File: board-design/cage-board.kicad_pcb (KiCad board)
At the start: 2 copper layers, 160 x 160 mm, 34 parts, among them J1 Jack-DC, J10 73131-0240, J11 73131-0240, J12 73131-0240, J13 Conn_01x02, J14 Conn_01x02, J15 Conn_02x13_test_points, J2 Conn_02x17_Ribbon, J3 TB002-500-03BE, J4 73131-0240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

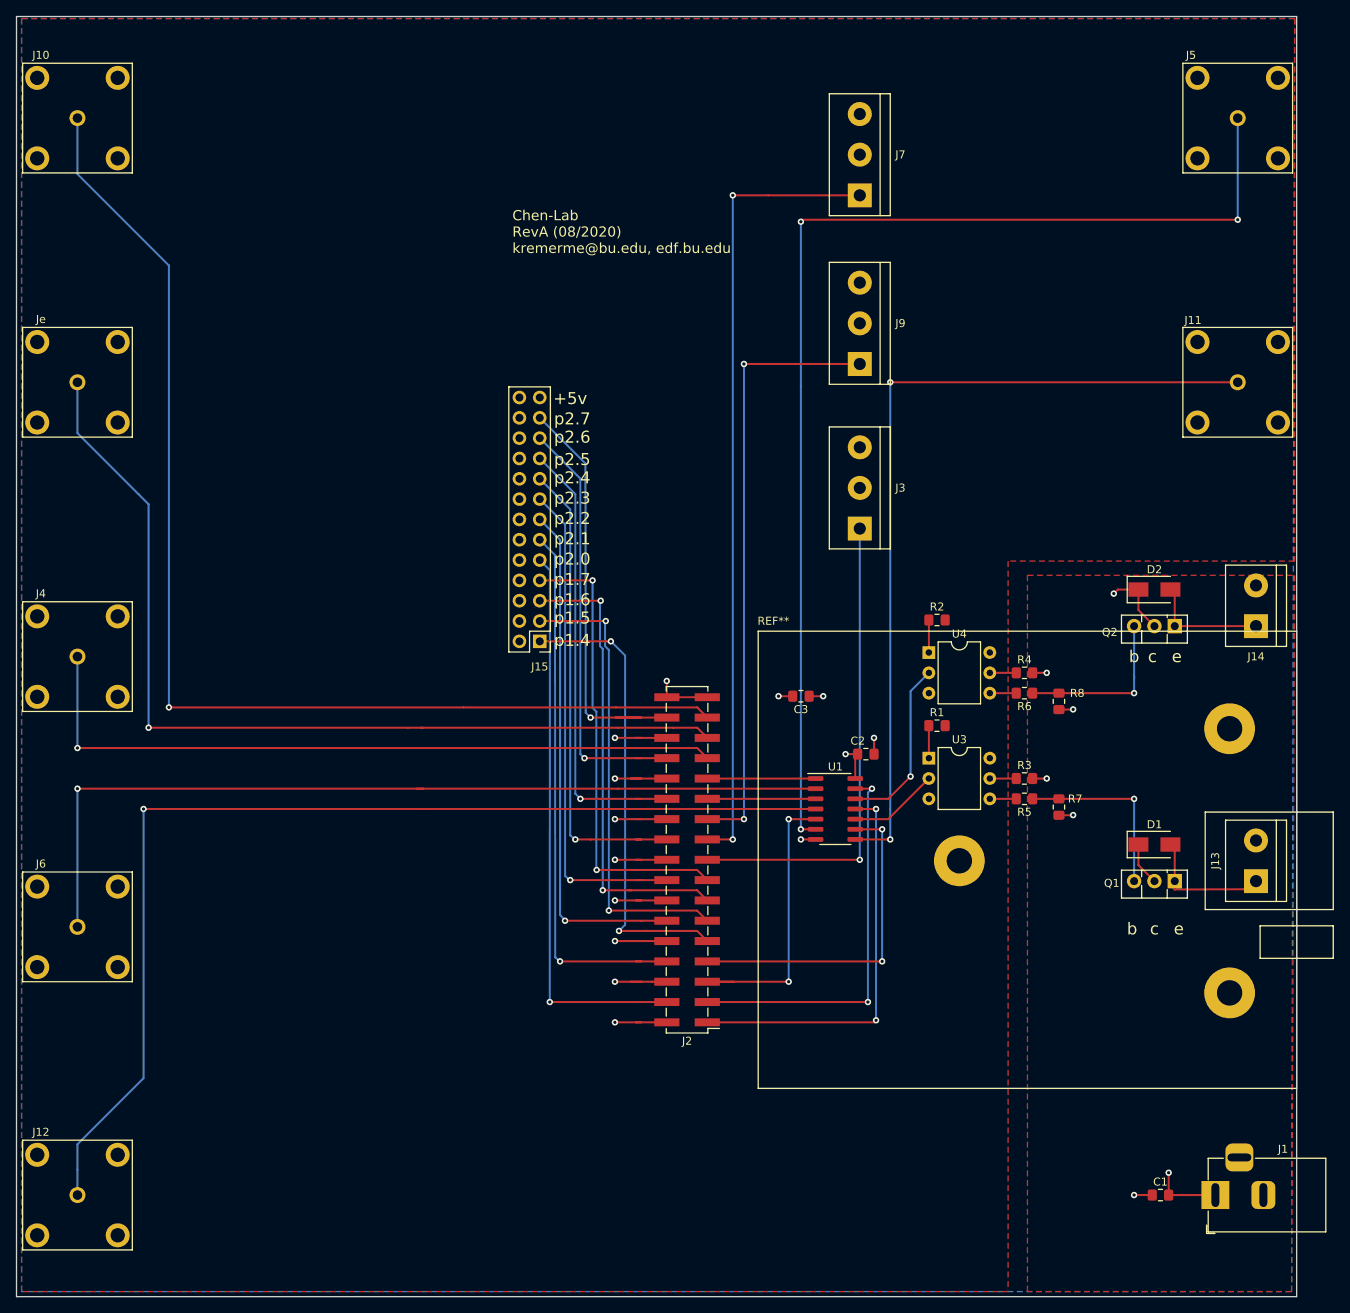
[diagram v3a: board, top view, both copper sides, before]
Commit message: updating schematic, and moving PCB layout forward to RevB
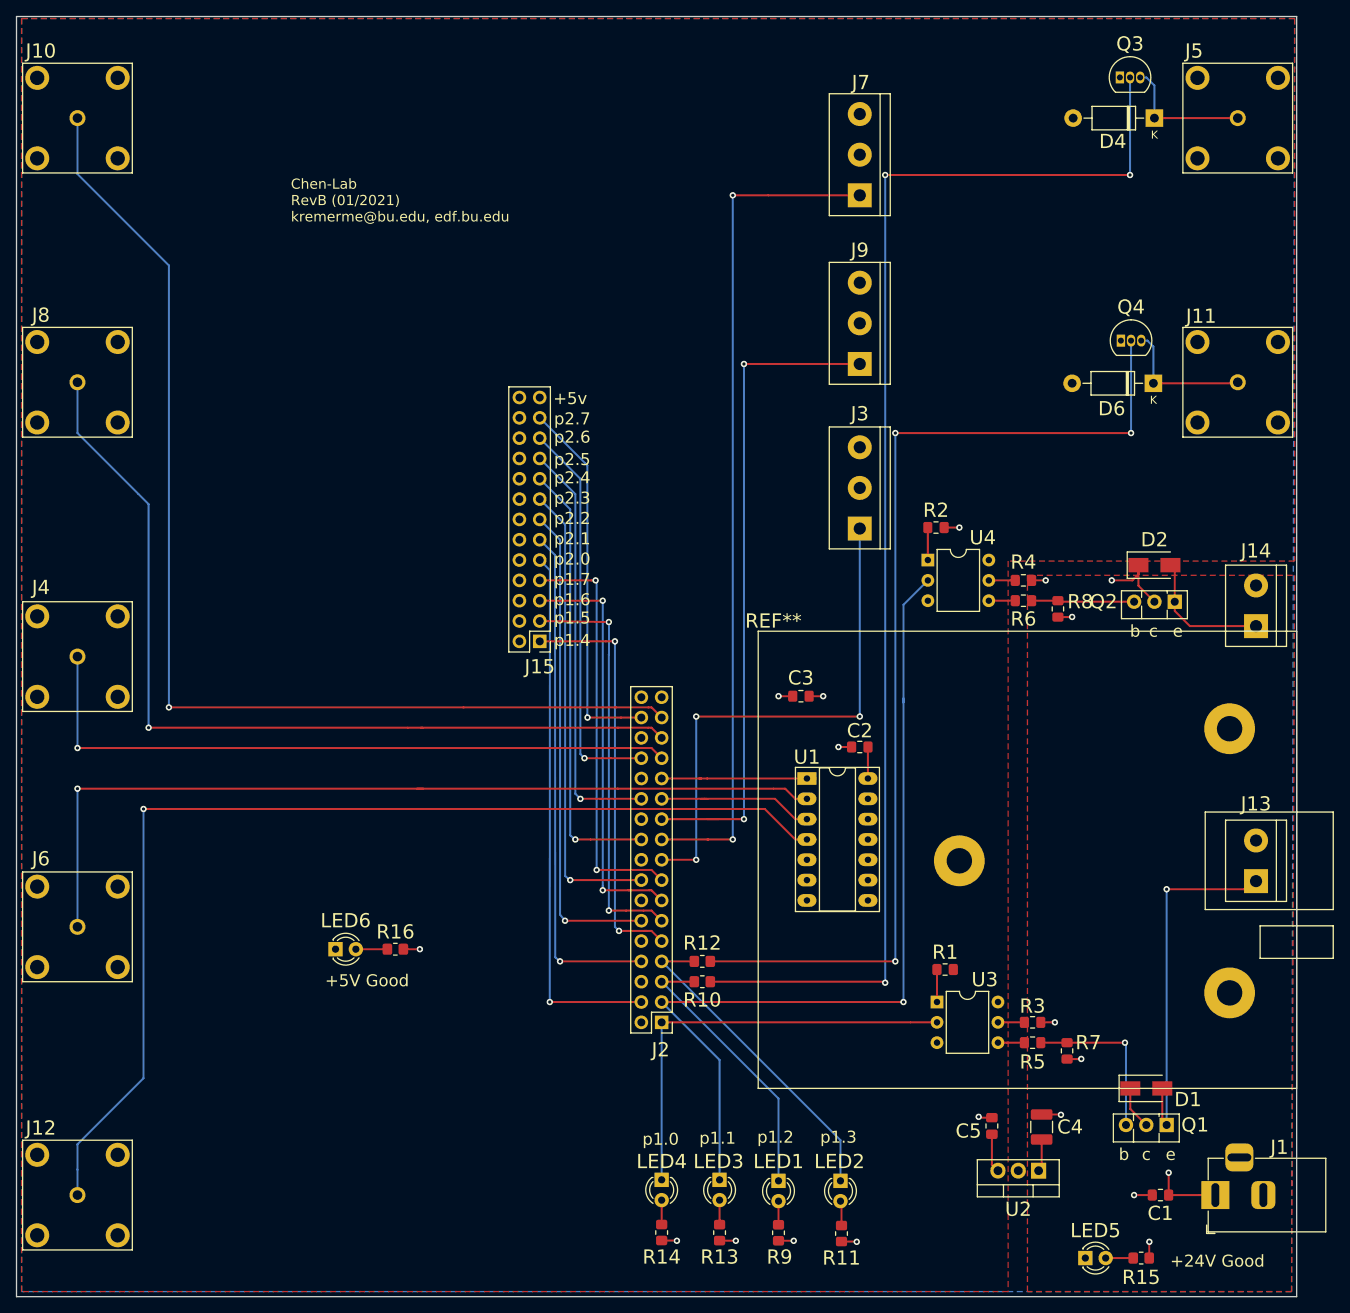
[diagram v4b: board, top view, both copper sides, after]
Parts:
- added C4: 10u 50V, Capacitor_SMD:C_1210_3225Metric_Pad1.33x2.70mm_HandSolder, F.Cu at (171.3, 138.8)
- added C5: 22u 10V, Capacitor_SMD:C_0805_2012Metric_Pad1.18x1.45mm_HandSolder, F.Cu at (165.1, 138.7)
- added D4: 1N4007, Diode_THT:D_DO-41_SOD81_P10.16mm_Horizontal, F.Cu at (185.4, 12.7)
- added D6: 1N4007, Diode_THT:D_DO-41_SOD81_P10.16mm_Horizontal, F.Cu at (185.3, 45.8)
- added LED1: LED, LED_THT:LED_D3.0mm, F.Cu at (138.4, 145.5)
- added LED2: LED, LED_THT:LED_D3.0mm, F.Cu at (146.2, 145.5)
- added LED3: LED, LED_THT:LED_D3.0mm, F.Cu at (131.1, 145.4)
- added LED4: LED, LED_THT:LED_D3.0mm, F.Cu at (123.8, 145.4)
- added LED5: LED, LED_THT:LED_D3.0mm, F.Cu at (176.8, 155.2)
- added LED6: LED, LED_THT:LED_D3.0mm, F.Cu at (83.1, 116.6)
- added Q3: 2N3906, Package_TO_SOT_THT:TO-92_Inline, F.Cu at (181.1, 7.62)
- added Q4: 2N3906, Package_TO_SOT_THT:TO-92_Inline, F.Cu at (181.2, 40.5)
- added R10: R_US, Resistor_SMD:R_0805_2012Metric_Pad1.20x1.40mm_HandSolder, F.Cu at (128.9, 120.7)
- added R11: 200, Resistor_SMD:R_0805_2012Metric_Pad1.20x1.40mm_HandSolder, F.Cu at (146.3, 152.1)
- added R12: R_US, Resistor_SMD:R_0805_2012Metric_Pad1.20x1.40mm_HandSolder, F.Cu at (128.9, 118.1)
- added R13: 200, Resistor_SMD:R_0805_2012Metric_Pad1.20x1.40mm_HandSolder, F.Cu at (131.1, 152.0)
- added R14: 200, Resistor_SMD:R_0805_2012Metric_Pad1.20x1.40mm_HandSolder, F.Cu at (123.8, 152.0)
- added R15: 1k, Resistor_SMD:R_0805_2012Metric_Pad1.20x1.40mm_HandSolder, F.Cu at (183.8, 155.2)
- added R16: 200, Resistor_SMD:R_0805_2012Metric_Pad1.20x1.40mm_HandSolder, F.Cu at (90.5, 116.6)
- added R9: 200, Resistor_SMD:R_0805_2012Metric_Pad1.20x1.40mm_HandSolder, F.Cu at (138.4, 152.0)
- added U2: VX7805-500, Package_TO_SOT_THT:TO-220-3_Vertical, F.Cu at (170.9, 144.3)
- J2: footprint Connector_PinHeader_2.54mm:PinHeader_2x17_P2.54mm_Vertical_SMD -> Connector_PinHeader_2.54mm:PinHeader_2x17_P2.54mm_Vertical
- U1: value 74LS06 -> 74HC04; footprint Package_SO:SOIC-14_3.9x8.7mm_P1.27mm -> Package_DIP:DIP-14_W7.62mm_Socket_LongPads
- U3, U4: value ERJ-UP8F6200V -> 4N25
- moved D1 30.5 mm to (184.4, 134.0)
- moved R1 30.5 mm to (159.3, 119.1)
- moved R3 30.5 mm to (170.2, 125.7)
- moved R5 30.5 mm to (170.2, 128.3)
- moved U3 30.5 mm to (158.2, 123.2)
- moved Q1 30.5 mm to (186.9, 138.6)
- moved R7 30.5 mm to (174.5, 129.3)
- moved J2 20.6 mm to (123.8, 125.7)
- moved R4 11.6 mm to (169.0, 70.5)
- moved R8 11.6 mm to (173.4, 74.0)
- moved U4 11.6 mm to (157.1, 67.9)
- moved R2 11.6 mm to (158.1, 63.9)
- moved R6 11.6 mm to (169.0, 73.0)
- moved U1 5.21 mm to (142.0, 95.2)
- moved D2 3.05 mm to (185.4, 68.6)
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- renumbered Je to J8
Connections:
- J11 pad 1: Net-(J11-Pad1) -> Net-(D6-Pad1)
- J2 pad 33: +5V -> Net-(J2-Pad33)
- J2 pad 34: +5V -> Net-(J2-Pad34)
- J5 pad 1: Net-(J5-Pad1) -> Net-(D4-Pad1)
- U1 pad 11: /P1.0 -> GND
- U1 pad 13: /P1.1 -> GND
- U1 pad 5: /P1.2 -> GND
- U1 pad 6: Net-(J5-Pad1) -> Net-(U1-Pad6)
- U1 pad 8: Net-(J11-Pad1) -> Net-(U1-Pad8)
- U1 pad 9: /P1.3 -> GND
- U3 pad 2: Net-(U1-Pad10) -> /P1.0
- U4 pad 2: Net-(U1-Pad12) -> /P1.1
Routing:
- net Net-(Q3-Pad2): track 0.00 -> 166.3 mm, vias 0 -> 3
- net Net-(J5-Pad1): track 145.2 -> 0.00 mm, vias 3 -> 0
- net Net-(Q4-Pad2): track 0.00 -> 130.8 mm, vias 0 -> 3
- net Net-(J11-Pad1): track 104.8 -> 0.00 mm, vias 2 -> 0
- net /P1.1: track 49.0 -> 109.9 mm, vias 2 -> 1
- net GND: track 69.9 -> 14.0 mm, vias 14 -> 7
- net Net-(D1-Pad2): track 16.0 -> 48.5 mm, vias 0 -> 1
- net Net-(U1-Pad12): track 22.0 -> 0.00 mm, vias 1 -> 0
- net Net-(D6-Pad1): track 0.00 -> 17.0 mm
- net Net-(D4-Pad1): track 0.00 -> 16.7 mm
- net Net-(U1-Pad10): track 11.3 -> 0.00 mm
- net Net-(Q2-Pad3): track 21.8 -> 12.9 mm, vias 1 -> 0
- net +5V: track 13.5 -> 22.3 mm, vias 3 -> 7
- net +24V: track 26.2 -> 33.8 mm, vias 4 -> 5
- net /P0.3: track 14.3 -> 21.8 mm
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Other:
- board text added: "+24V Good"
- board text added: "+5V Good"
- board text added: "Chen-Lab RevB (01/2021) kremerme@bu.edu, edf.bu.edu"
- board text added: "p1.0"
- board text added: "p1.1"
- board text added: "p1.2"
- board text added: "p1.3"
- board text removed: "Chen-Lab RevA (08/2020) kremerme@bu.edu, edf.bu.edu"

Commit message: auto push run at Fri Apr  9 11:10:50 EDT 2021
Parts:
- added J16: TB002-500-03BE, TerminalBlock:TerminalBlock_bornier-3_P5.08mm, F.Cu at (126.4, 64.1)
- added J17: TB002-500-03BE, TerminalBlock:TerminalBlock_bornier-3_P5.08mm, F.Cu at (126.4, 43.2)
- added J18: TB002-500-03BE, TerminalBlock:TerminalBlock_bornier-3_P5.08mm, F.Cu at (126.4, 22.2)
- R10, R12: value R_US -> 1.5k
- moved J15 8.25 mm to (100.3, 78.1)
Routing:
- net /P2.2: track 61.0 -> 136.6 mm, vias 1 -> 3
- net /P2.1: track 63.9 -> 124.3 mm, vias 1 -> 3
- net /P2.0: track 67.2 -> 105.6 mm
- net /P2.4: track 55.2 -> 66.7 mm
- net /P1.5: track 51.8 -> 61.4 mm
- net /P2.3: track 58.2 -> 67.7 mm
- net /P2.5: track 52.3 -> 61.8 mm
- net /P1.6: track 52.3 -> 61.6 mm
- net /P1.4: track 51.9 -> 61.1 mm
- net /P2.6: track 49.3 -> 58.2 mm
- net /P2.7: track 46.7 -> 54.9 mm
- net /P1.7: track 52.1 -> 60.2 mm

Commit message: auto push run at Fri Apr  9 12:23:24 EDT 2021
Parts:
- D1, D2: value D_Small -> 1N4007; footprint Diode_SMD:D_SMA -> Diode_THT:D_DO-41_SOD81_P10.16mm_Horizontal
- R11, R13, R14, R16, R9: value 200 -> 1k
- R15: value 1k -> 10k
- moved J16 10.2 mm to (126.4, 54.0), turned to 270 degrees
- moved J18 10.2 mm to (126.4, 12.1), turned to 270 degrees
- moved J17 10.2 mm to (126.4, 33.0), turned to 270 degrees
- moved D1 7.90 mm to (176.5, 134.6)
- moved D2 7.85 mm to (177.8, 66.7)
- moved R2 3.65 mm to (161.5, 62.6)
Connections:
- J16 pad 1: /P2.0 -> +5V
- J16 pad 2: +5V -> GND
- J16 pad 3: GND -> /P2.0
- J17 pad 1: /P2.1 -> +5V
- J17 pad 2: +5V -> GND
- J17 pad 3: GND -> /P2.1
- J18 pad 1: /P2.2 -> +5V
- J18 pad 2: +5V -> GND
- J18 pad 3: GND -> /P2.2
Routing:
- net +24V: track 33.8 -> 28.4 mm
- net Net-(D1-Pad2): track 48.5 -> 45.3 mm
- net Net-(R2-Pad1): track 4.06 -> 6.75 mm
- net Net-(D2-Pad2): track 16.9 -> 18.7 mm
- net +5V: track 22.3 -> 23.1 mm
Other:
- board text added: "GND"
- board text added: "p0.0"
- board text added: "p0.1"
- board text added: "p0.2"
